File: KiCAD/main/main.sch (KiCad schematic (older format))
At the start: 10 parts, among them IC1 DHT22, J1 Charge controller, J2 Sound Sensor, J3 BuckConverter, J4 Anemometer, U1 4020, U1 4N25

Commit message: Clear anotations
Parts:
- renumbered IC1 to IC?, J3 to J?, J2 to J?, J4 to J?, J1 to J?, R2 to R?, R3 to R?, U1 to U?
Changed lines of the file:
@@
 	9250 2700 9650 2700
 $Comp
-L Connector_Generic:Conn_01x04 J3
+L Connector_Generic:Conn_01x04 J?
 U 1 1 5FC4DC93
 P 1000 3700
-F 0 "J3" H 918 4017 50  0000 C CNN
+F 0 "J?" H 918 4017 50  0000 C CNN
 F 1 "BuckConverter" H 918 3926 50  0000 C CNN
 F 2 "Connector_PinSocket_2.54mm:PinSocket_1x04_P2.54mm_Vertical" H 1000 3700 50  0001 C CNN
@@
 NoConn ~ 1350 3600
 $Comp
-L Connector_Generic:Conn_01x04 J2
+L Connector_Generic:Conn_01x04 J?
 U 1 1 5FC5154E
 P 1000 1850
-F 0 "J2" H 918 2167 50  0000 C CNN
+F 0 "J?" H 918 2167 50  0000 C CNN
 F 1 "Sound Sensor" H 918 2076 50  0000 C CNN
 F 2 "Connector_JST:JST_PH_B4B-PH-K_1x04_P2.00mm_Vertical" H 1000 1850 50  0001 C CNN
@@
 	1550 2800 1250 2800
 $Comp
-L Connector_Generic:Conn_01x02 J4
+L Connector_Generic:Conn_01x02 J?
 U 1 1 5FC61584
 P 9850 2600
-F 0 "J4" H 9930 2592 50  0000 L CNN
+F 0 "J?" H 9930 2592 50  0000 L CNN
 F 1 "Anemometer" H 9930 2501 50  0000 L CNN
 F 2 "Connector_JST:JST_PH_B2B-PH-K_1x02_P2.00mm_Vertical" H 9850 2600 50  0001 C CNN
@@
 	8350 3700 8150 3700
 $Comp
-L DHT22:DHT22 IC1
+L DHT22:DHT22 IC?
 U 1 1 5FB3BE3A
 P 8350 3600
-F 0 "IC1" H 8692 3035 50  0000 C CNN
+F 0 "IC?" H 8692 3035 50  0000 C CNN
 F 1 "DHT22" H 8692 3126 50  0000 C CNN
 F 2 "DHT22" H 9100 3700 50  0001 L CNN
@@
 $EndSheet
 $Comp
-L 4xxx:4020 U1
+L 4xxx:4020 U?
 U 1 1 5FCB685F
 P 5200 3350
-F 0 "U1" H 5200 4331 50  0000 C CNN
+F 0 "U?" H 5200 4331 50  0000 C CNN
 F 1 "4020" H 5200 4240 50  0000 C CNN
 F 2 "Package_DIP:DIP-16_W7.62mm_LongPads" H 5200 3350 50  0001 C CNN
@@
 VDD
 $Comp
-L Device:R R3
+L Device:R R?
 U 1 1 5FCAD4DB
 P 7150 2550
-F 0 "R3" H 7220 2596 50  0000 L CNN
+F 0 "R?" H 7220 2596 50  0000 L CNN
 F 1 "10k" H 7220 2505 50  0000 L CNN
 F 2 "Resistor_SMD:R_1206_3216Metric" V 7080 2550 50  0001 C CNN
@@
 	7900 2400 8100 2400
 $Comp
-L Device:R R2
+L Device:R R?
 U 1 1 5FCA1125
 P 8050 2200
-F 0 "R2" V 7843 2200 50  0000 C CNN
+F 0 "R?" V 7843 2200 50  0000 C CNN
 F 1 "620" V 7934 2200 50  0000 C CNN
 F 2 "Resistor_SMD:R_1206_3216Metric" V 7980 2200 50  0001 C CNN
@@
 $EndComp
 $Comp
-L Isolator:4N25 U1
+L Isolator:4N25 U?
 U 1 1 5FC7ABC6
 P 7600 2300
-F 0 "U1" H 7600 2625 50  0000 C CNN
+F 0 "U?" H 7600 2625 50  0000 C CNN
 F 1 "4N25" H 7600 2534 50  0000 C CNN
 F 2 "Package_DIP:DIP-6_W7.62mm_LongPads" H 7400 2100 50  0001 L CIN
@@
 Battery_status
 $Comp
-L Connector_Generic:Conn_01x03 J1
+L Connector_Generic:Conn_01x03 J?
 U 1 1 5FCA41A5
 P 1050 2800
-F 0 "J1" H 968 3117 50  0000 C CNN
+F 0 "J?" H 968 3117 50  0000 C CNN
 F 1 "Charge controller" H 968 3026 50  0000 C CNN
 F 2 "" H 1050 2800 50  0001 C CNN

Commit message: Reanotate everything and assign missing footprints
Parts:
- IC1: renamed from IC?; footprint DHT22 -> Local:DHT22
- J3: renamed from J?; footprint (none) -> Connector_JST:JST_PH_B3B-PH-K_1x03_P2.00mm_Vertical
- gave numbers to parts that had none: 8
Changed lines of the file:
@@
 	9250 2700 9650 2700
 $Comp
-L Connector_Generic:Conn_01x04 J?
+L Connector_Generic:Conn_01x04 J2
 U 1 1 5FC4DC93
 P 1000 3700
-F 0 "J?" H 918 4017 50  0000 C CNN
+F 0 "J2" H 918 4017 50  0000 C CNN
 F 1 "BuckConverter" H 918 3926 50  0000 C CNN
 F 2 "Connector_PinSocket_2.54mm:PinSocket_1x04_P2.54mm_Vertical" H 1000 3700 50  0001 C CNN
@@
 NoConn ~ 1350 3600
 $Comp
-L Connector_Generic:Conn_01x04 J?
+L Connector_Generic:Conn_01x04 J1
 U 1 1 5FC5154E
 P 1000 1850
-F 0 "J?" H 918 2167 50  0000 C CNN
+F 0 "J1" H 918 2167 50  0000 C CNN
 F 1 "Sound Sensor" H 918 2076 50  0000 C CNN
 F 2 "Connector_JST:JST_PH_B4B-PH-K_1x04_P2.00mm_Vertical" H 1000 1850 50  0001 C CNN
@@
 	1550 2800 1250 2800
 $Comp
-L Connector_Generic:Conn_01x02 J?
+L Connector_Generic:Conn_01x02 J4
 U 1 1 5FC61584
 P 9850 2600
-F 0 "J?" H 9930 2592 50  0000 L CNN
+F 0 "J4" H 9930 2592 50  0000 L CNN
 F 1 "Anemometer" H 9930 2501 50  0000 L CNN
 F 2 "Connector_JST:JST_PH_B2B-PH-K_1x02_P2.00mm_Vertical" H 9850 2600 50  0001 C CNN
@@
 	8350 3700 8150 3700
 $Comp
-L DHT22:DHT22 IC?
+L DHT22:DHT22 IC1
 U 1 1 5FB3BE3A
 P 8350 3600
-F 0 "IC?" H 8692 3035 50  0000 C CNN
+F 0 "IC1" H 8692 3035 50  0000 C CNN
 F 1 "DHT22" H 8692 3126 50  0000 C CNN
-F 2 "DHT22" H 9100 3700 50  0001 L CNN
+F 2 "Local:DHT22" H 9100 3700 50  0001 L CNN
 F 3 "https://datasheet4u.com/datasheet-parts/DHT22-datasheet.php?id=792211" H 9100 3600 50  0001 L CNN
 F 4 "Digital-output relative humidity & temperature sensor/module DHT22" H 9100 3500 50  0001 L CNN "Description"
@@
 $EndSheet
 $Comp
-L 4xxx:4020 U?
+L 4xxx:4020 U1
 U 1 1 5FCB685F
 P 5200 3350
-F 0 "U?" H 5200 4331 50  0000 C CNN
+F 0 "U1" H 5200 4331 50  0000 C CNN
 F 1 "4020" H 5200 4240 50  0000 C CNN
 F 2 "Package_DIP:DIP-16_W7.62mm_LongPads" H 5200 3350 50  0001 C CNN
@@
 VDD
 $Comp
-L Device:R R?
+L Device:R R1
 U 1 1 5FCAD4DB
 P 7150 2550
-F 0 "R?" H 7220 2596 50  0000 L CNN
+F 0 "R1" H 7220 2596 50  0000 L CNN
 F 1 "10k" H 7220 2505 50  0000 L CNN
 F 2 "Resistor_SMD:R_1206_3216Metric" V 7080 2550 50  0001 C CNN
@@
 	7900 2400 8100 2400
 $Comp
-L Device:R R?
+L Device:R R2
 U 1 1 5FCA1125
 P 8050 2200
-F 0 "R?" V 7843 2200 50  0000 C CNN
+F 0 "R2" V 7843 2200 50  0000 C CNN
 F 1 "620" V 7934 2200 50  0000 C CNN
 F 2 "Resistor_SMD:R_1206_3216Metric" V 7980 2200 50  0001 C CNN
@@
 $EndComp
 $Comp
-L Isolator:4N25 U?
+L Isolator:4N25 U2
 U 1 1 5FC7ABC6
 P 7600 2300
-F 0 "U?" H 7600 2625 50  0000 C CNN
+F 0 "U2" H 7600 2625 50  0000 C CNN
 F 1 "4N25" H 7600 2534 50  0000 C CNN
 F 2 "Package_DIP:DIP-6_W7.62mm_LongPads" H 7400 2100 50  0001 L CIN
@@
 Battery_status
 $Comp
-L Connector_Generic:Conn_01x03 J?
+L Connector_Generic:Conn_01x03 J3
 U 1 1 5FCA41A5
 P 1050 2800
-F 0 "J?" H 968 3117 50  0000 C CNN
+F 0 "J3" H 968 3117 50  0000 C CNN
 F 1 "Charge controller" H 968 3026 50  0000 C CNN
-F 2 "" H 1050 2800 50  0001 C CNN
+F 2 "Connector_JST:JST_PH_B3B-PH-K_1x03_P2.00mm_Vertical" H 1050 2800 50  0001 C CNN
 F 3 "~" H 1050 2800 50  0001 C CNN
 	1    1050 2800
@@
 	1250 2700 1900 2700
 $Comp
-L Switch:SW_SPDT SW?
+L Switch:SW_SPDT SW1
 U 1 1 5FCD21D1
 P 2100 2500
-F 0 "SW?" H 2100 2785 50  0000 C CNN
+F 0 "SW1" H 2100 2785 50  0000 C CNN
 F 1 "SW_SPDT" H 2100 2694 50  0000 C CNN
 F 2 "Button_Switch_THT:SW_CuK_OS102011MA1QN1_SPDT_Angled" H 2100 2500 50  0001 C CNN

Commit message: Fix battery charger connectors
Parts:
- removed J3: Charge controller, Connector_JST:JST_PH_B3B-PH-K_1x03_P2.00mm_Vertical, symbol Connector_Generic:Conn_01x03
- added J3: Charge Controller, Connector_JST:JST_PH_B2B-PH-K_1x02_P2.00mm_Vertical, symbol Connector_Generic:Conn_01x02
- added J4: Battery Status, Connector_PinHeader_2.54mm:PinHeader_1x01_P2.54mm_Vertical, symbol Connector_Generic:Conn_01x01
- renumbered J4 to J5
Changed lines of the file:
@@
 	1550 2800 1250 2800
 $Comp
-L Connector_Generic:Conn_01x02 J4
+L Connector_Generic:Conn_01x02 J5
 U 1 1 5FC61584
 P 9850 2600
-F 0 "J4" H 9930 2592 50  0000 L CNN
+F 0 "J5" H 9930 2592 50  0000 L CNN
 F 1 "Anemometer" H 9930 2501 50  0000 L CNN
 F 2 "Connector_JST:JST_PH_B2B-PH-K_1x02_P2.00mm_Vertical" H 9850 2600 50  0001 C CNN
@@
 Text Label 2900 3750 2    50   ~ 0
 Battery_status
-$Comp
-L Connector_Generic:Conn_01x03 J3
-U 1 1 5FCA41A5
-P 1050 2800
-F 0 "J3" H 968 3117 50  0000 C CNN
-F 1 "Charge controller" H 968 3026 50  0000 C CNN
-F 2 "Connector_JST:JST_PH_B3B-PH-K_1x03_P2.00mm_Vertical" H 1050 2800 50  0001 C CNN
-F 3 "~" H 1050 2800 50  0001 C CNN
-	1    1050 2800
-	-1   0    0    -1
-$EndComp
-Wire Wire Line
-	1250 2900 1550 2900
-Text Label 1550 2900 0    50   ~ 0
+Wire Wire Line
+	1250 3100 1550 3100
+Text Label 1550 3100 0    50   ~ 0
 Battery_status
 Wire Wire Line
@@
 	1    0    0    -1
 $EndComp
+$Comp
+L Connector_Generic:Conn_01x02 J3
+U 1 1 5FD1D628
+P 1050 2700
+F 0 "J3" H 968 2917 50  0000 C CNN
+F 1 "Charge Controller" H 968 2826 50  0000 C CNN
+F 2 "Connector_JST:JST_PH_B2B-PH-K_1x02_P2.00mm_Vertical" H 1050 2700 50  0001 C CNN
+F 3 "~" H 1050 2700 50  0001 C CNN
+	1    1050 2700
+	-1   0    0    -1
+$EndComp
+$Comp
+L Connector_Generic:Conn_01x01 J4
+U 1 1 5FD1E1C3
+P 1050 3100
+F 0 "J4" H 968 3317 50  0000 C CNN
+F 1 "Battery Status" H 968 3226 50  0000 C CNN
+F 2 "Connector_PinHeader_2.54mm:PinHeader_1x01_P2.54mm_Vertical" H 1050 3100 50  0001 C CNN
+F 3 "~" H 1050 3100 50  0001 C CNN
+	1    1050 3100
+	-1   0    0    -1
+$EndComp
 $EndSCHEMATC

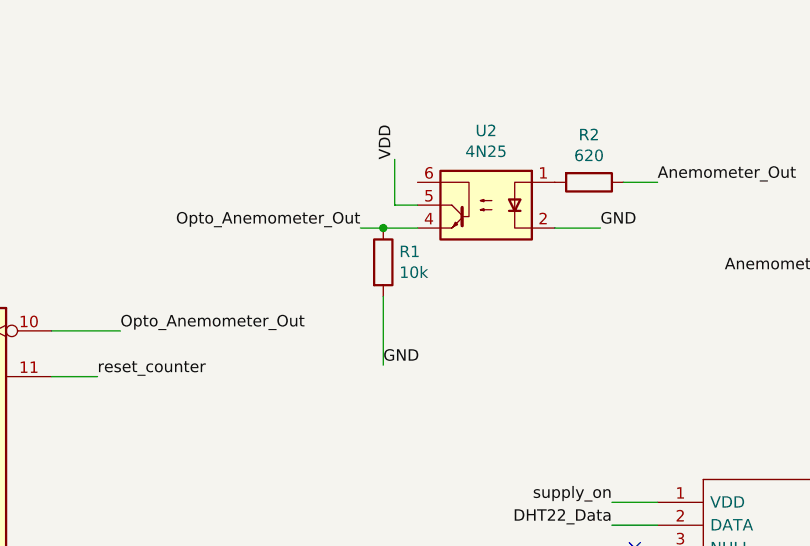
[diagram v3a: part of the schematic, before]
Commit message: Preliminary layout with fixed component pins
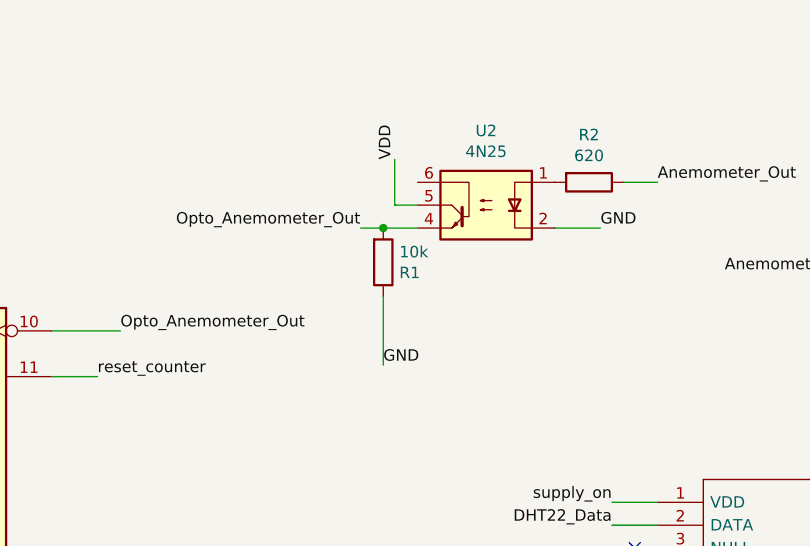
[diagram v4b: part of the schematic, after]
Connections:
- net GND: now also R1.1; no longer R1.2
- net Opto_Anemometer_Out: now also R1.2; no longer R1.1
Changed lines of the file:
@@
 F 3 "~" H 7150 2550 50  0001 C CNN
 	1    7150 2550
-	1    0    0    -1
+	1    0    0    1
 $EndComp
 Text Label 6000 2850 0    50   ~ 0

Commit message: Change ON switch footprint
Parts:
- SW1: footprint Button_Switch_THT:SW_CuK_OS102011MA1QN1_SPDT_Angled -> Button_Switch_THT:SW_CuK_JS202011AQN_DPDT_Angled
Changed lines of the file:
@@
 F 0 "SW1" H 2100 2785 50  0000 C CNN
 F 1 "SW_SPDT" H 2100 2694 50  0000 C CNN
-F 2 "Button_Switch_THT:SW_CuK_OS102011MA1QN1_SPDT_Angled" H 2100 2500 50  0001 C CNN
+F 2 "Button_Switch_THT:SW_CuK_JS202011AQN_DPDT_Angled" H 2100 2500 50  0001 C CNN
 F 3 "~" H 2100 2500 50  0001 C CNN
 	1    2100 2500

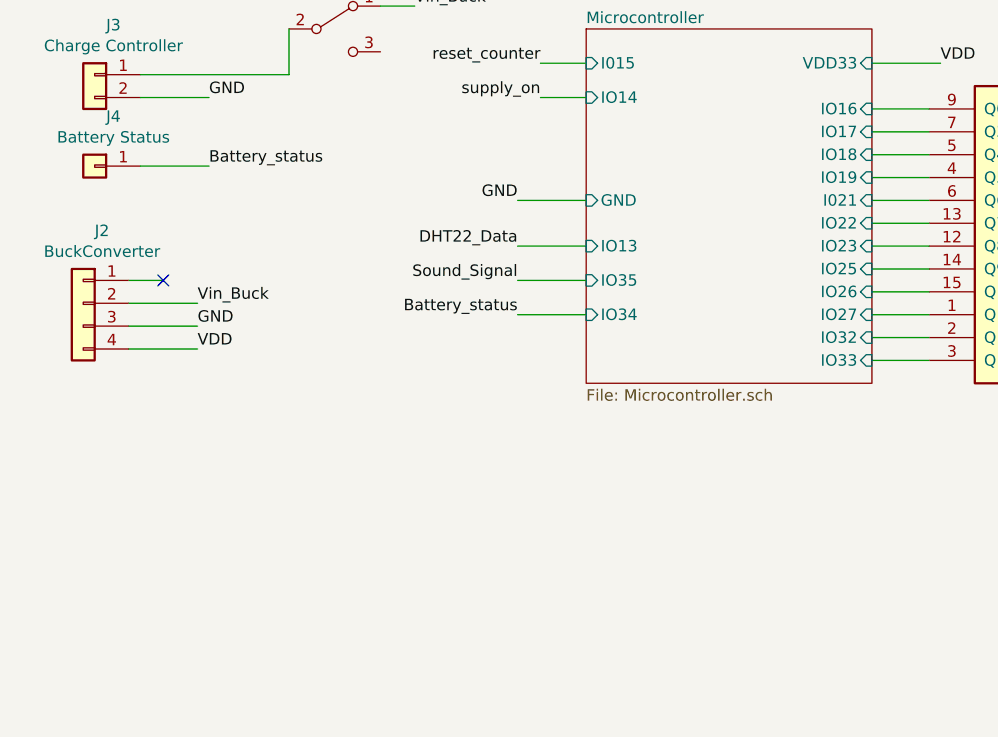
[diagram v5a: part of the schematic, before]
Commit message: Add some pcb test points
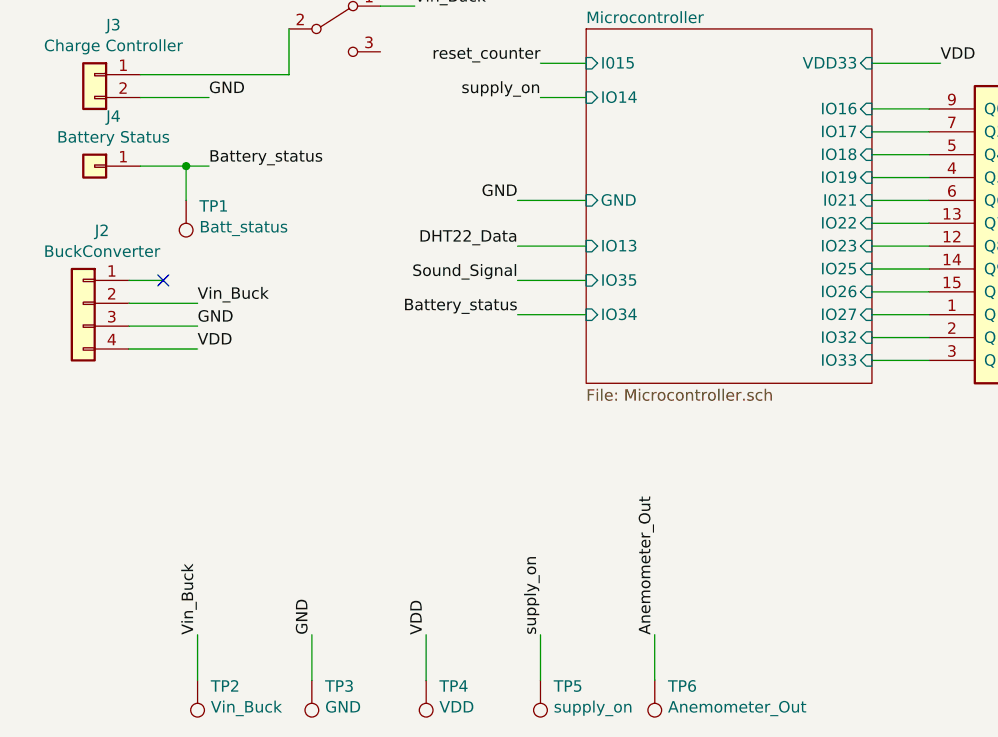
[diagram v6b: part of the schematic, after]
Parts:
- added TP1: Batt_status, TestPoint:TestPoint_Pad_1.0x1.0mm, symbol Connector:TestPoint
- added TP2: Vin_Buck, TestPoint:TestPoint_Pad_1.0x1.0mm, symbol Connector:TestPoint
- added TP3: GND, TestPoint:TestPoint_Pad_1.0x1.0mm, symbol Connector:TestPoint
- added TP4: VDD, TestPoint:TestPoint_Pad_1.0x1.0mm, symbol Connector:TestPoint
- added TP5: supply_on, TestPoint:TestPoint_Pad_1.0x1.0mm, symbol Connector:TestPoint
- added TP6: Anemometer_Out, TestPoint:TestPoint_Pad_1.0x1.0mm, symbol Connector:TestPoint
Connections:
- net Anemometer_Out: now also TP6.1
- net Battery_status: now also TP1.1
- net GND: now also TP3.1
- net VDD: now also TP4.1
- net Vin_Buck: now also TP2.1
- net supply_on: now also TP5.1
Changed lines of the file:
@@
 Text Label 2900 3750 2    50   ~ 0
 Battery_status
-Wire Wire Line
-	1250 3100 1550 3100
 Text Label 1550 3100 0    50   ~ 0
 Battery_status
@@
 	-1   0    0    -1
 $EndComp
+Wire Wire Line
+	1250 3100 1450 3100
+$Comp
+L Connector:TestPoint TP1
+U 1 1 5FDCB7BA
+P 1450 3250
+F 0 "TP1" H 1392 3276 50  0000 R CNN
+F 1 "Batt_status" H 1392 3367 50  0000 R CNN
+F 2 "TestPoint:TestPoint_Pad_1.0x1.0mm" H 1650 3250 50  0001 C CNN
+F 3 "~" H 1650 3250 50  0001 C CNN
+	1    1450 3250
+	-1   0    0    1
+$EndComp
+Wire Wire Line
+	1450 3250 1450 3100
+Connection ~ 1450 3100
+Wire Wire Line
+	1450 3100 1550 3100
+$Comp
+L Connector:TestPoint TP2
+U 1 1 5FDCD96A
+P 1500 5350
+F 0 "TP2" H 1442 5376 50  0000 R CNN
+F 1 "Vin_Buck" H 1442 5467 50  0000 R CNN
+F 2 "TestPoint:TestPoint_Pad_1.0x1.0mm" H 1700 5350 50  0001 C CNN
+F 3 "~" H 1700 5350 50  0001 C CNN
+	1    1500 5350
+	-1   0    0    1
+$EndComp
+Wire Wire Line
+	1500 5350 1500 5150
+Text Label 1500 5150 1    50   ~ 0
+Vin_Buck
+$Comp
+L Connector:TestPoint TP3
+U 1 1 5FDD2E43
+P 2000 5350
+F 0 "TP3" H 1942 5376 50  0000 R CNN
+F 1 "GND" H 1942 5467 50  0000 R CNN
+F 2 "TestPoint:TestPoint_Pad_1.0x1.0mm" H 2200 5350 50  0001 C CNN
+F 3 "~" H 2200 5350 50  0001 C CNN
+	1    2000 5350
+	-1   0    0    1
+$EndComp
+Wire Wire Line
+	2000 5150 2000 5350
+Text Label 2000 5150 1    50   ~ 0
+GND
+$Comp
+L Connector:TestPoint TP4
+U 1 1 5FDD4966
+P 2500 5350
+F 0 "TP4" H 2442 5376 50  0000 R CNN
+F 1 "VDD" H 2442 5467 50  0000 R CNN
+F 2 "TestPoint:TestPoint_Pad_1.0x1.0mm" H 2700 5350 50  0001 C CNN
+F 3 "~" H 2700 5350 50  0001 C CNN
+	1    2500 5350
+	-1   0    0    1
+$EndComp
+Wire Wire Line
+	2500 5350 2500 5150
+Text Label 2500 5150 1    50   ~ 0
+VDD
+$Comp
+L Connector:TestPoint TP5
+U 1 1 5FDD6353
+P 3000 5350
+F 0 "TP5" H 2942 5376 50  0000 R CNN
+F 1 "supply_on" H 2942 5467 50  0000 R CNN
+F 2 "TestPoint:TestPoint_Pad_1.0x1.0mm" H 3200 5350 50  0001 C CNN
+F 3 "~" H 3200 5350 50  0001 C CNN
+	1    3000 5350
+	-1   0    0    1
+$EndComp
+Wire Wire Line
+	3000 5350 3000 5150
+Text Label 3000 5150 1    50   ~ 0
+supply_on
+$Comp
+L Connector:TestPoint TP6
+U 1 1 5FDD7BC0
+P 3500 5350
+F 0 "TP6" H 3442 5376 50  0000 R CNN
+F 1 "Anemometer_Out" H 3442 5467 50  0000 R CNN
+F 2 "TestPoint:TestPoint_Pad_1.0x1.0mm" H 3700 5350 50  0001 C CNN
+F 3 "~" H 3700 5350 50  0001 C CNN
+	1    3500 5350
+	-1   0    0    1
+$EndComp
+Wire Wire Line
+	3500 5350 3500 5150
+Text Label 3500 5150 1    50   ~ 0
+Anemometer_Out
 $EndSCHEMATC

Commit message: Replace all possible footprints to THT variants
Also clear current PCB design and update component footprints
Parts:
- R1, R2: footprint Resistor_SMD:R_1206_3216Metric -> Resistor_THT:R_Axial_DIN0207_L6.3mm_D2.5mm_P10.16mm_Horizontal
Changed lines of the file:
@@
 F 0 "R1" H 7220 2596 50  0000 L CNN
 F 1 "10k" H 7220 2505 50  0000 L CNN
-F 2 "Resistor_SMD:R_1206_3216Metric" V 7080 2550 50  0001 C CNN
+F 2 "Resistor_THT:R_Axial_DIN0207_L6.3mm_D2.5mm_P10.16mm_Horizontal" V 7080 2550 50  0001 C CNN
 F 3 "~" H 7150 2550 50  0001 C CNN
 	1    7150 2550
@@
 F 0 "R2" V 7843 2200 50  0000 C CNN
 F 1 "620" V 7934 2200 50  0000 C CNN
-F 2 "Resistor_SMD:R_1206_3216Metric" V 7980 2200 50  0001 C CNN
+F 2 "Resistor_THT:R_Axial_DIN0207_L6.3mm_D2.5mm_P10.16mm_Horizontal" V 7980 2200 50  0001 C CNN
 F 3 "~" H 8050 2200 50  0001 C CNN
 	1    8050 2200

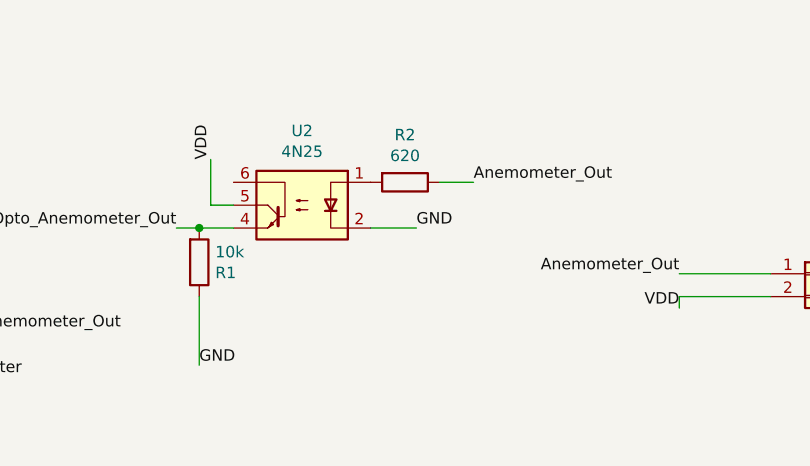
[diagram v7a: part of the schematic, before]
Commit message: Expand design vertically, reposition components and re-track
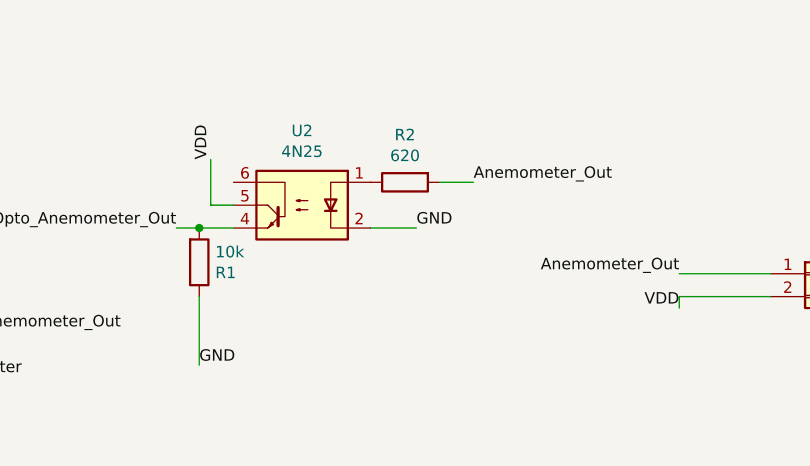
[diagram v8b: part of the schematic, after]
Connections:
- net Anemometer_Out: now also R2.2; no longer R2.1
- net at U2.1: now also R2.1; no longer R2.2
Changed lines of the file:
@@
 	7900 2400 8100 2400
-$Comp
-L Device:R R2
-U 1 1 5FCA1125
-P 8050 2200
-F 0 "R2" V 7843 2200 50  0000 C CNN
-F 1 "620" V 7934 2200 50  0000 C CNN
-F 2 "Resistor_THT:R_Axial_DIN0207_L6.3mm_D2.5mm_P10.16mm_Horizontal" V 7980 2200 50  0001 C CNN
-F 3 "~" H 8050 2200 50  0001 C CNN
-	1    8050 2200
-	0    1    1    0
-$EndComp
 $Comp
 L Isolator:4N25 U2
@@
 Text Label 3500 5150 1    50   ~ 0
 Anemometer_Out
+$Comp
+L Device:R R2
+U 1 1 5FCA1125
+P 8050 2200
+F 0 "R2" V 7843 2200 50  0000 C CNN
+F 1 "620" V 7934 2200 50  0000 C CNN
+F 2 "Resistor_THT:R_Axial_DIN0207_L6.3mm_D2.5mm_P10.16mm_Horizontal" V 7980 2200 50  0001 C CNN
+F 3 "~" H 8050 2200 50  0001 C CNN
+	1    8050 2200
+	0    -1   1    0
+$EndComp
 $EndSCHEMATC
